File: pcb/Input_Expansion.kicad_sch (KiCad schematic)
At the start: 3 parts, among them U2 MCP23008-xP

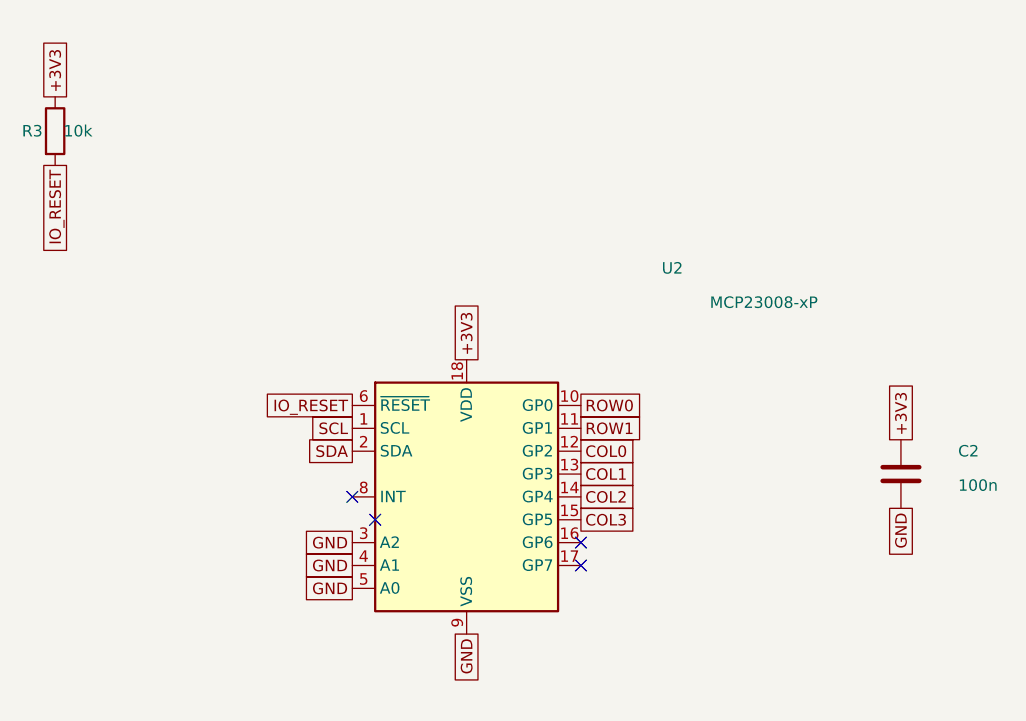
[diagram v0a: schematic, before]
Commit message: Updated wih cheeaper pads
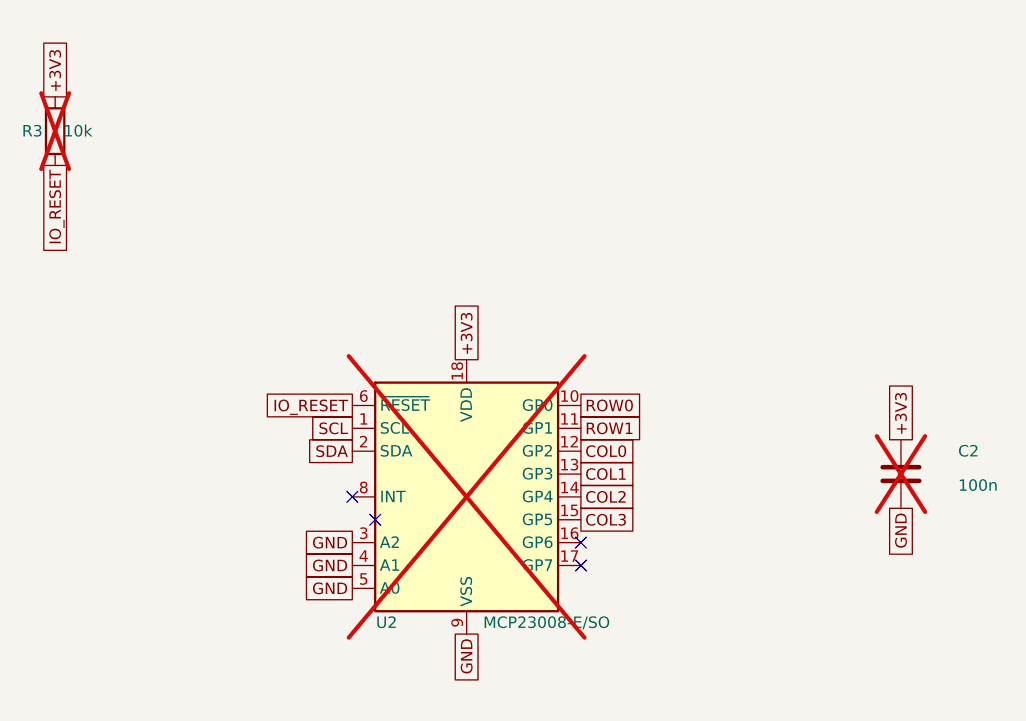
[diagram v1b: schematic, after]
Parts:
- removed U2: MCP23008-xP, Package_DIP:DIP-18_W7.62mm, symbol Interface_Expansion:MCP23008-xP
- added U2: MCP23008-E/SO, Package_SO:SOIC-18W_7.5x11.6mm_P1.27mm, symbol Interface_Expansion:MCP23008-xSO
- C2, R3: now not fitted
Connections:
- net +3V3: now also U2.18 (VDD)
- net COL0: now also U2.12 (GP2)
- net COL1: now also U2.13 (GP3)
- net COL2: now also U2.14 (GP4)
- net COL3: now also U2.15 (GP5)
- net GND: now also U2.3 (A2), U2.4 (A1), U2.5 (A0), U2.9 (VSS)
- net IO_RESET: now also U2.6 (~{RESET})
- net ROW0: now also U2.10 (GP0)
- net ROW1: now also U2.11 (GP1)
- net SCL: now also U2.1 (SCL)
- net SDA: now also U2.2 (SDA)
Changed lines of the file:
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@@
 	(paper "A4")
-	(symbol
-		(lib_id "Interface_Expansion:MCP23008-xP")
-		(at 116.84 88.9 0)
-		(unit 1)
-		(body_style 1)
-		(exclude_from_sim no)
-		(in_bom yes)
-		(on_board yes)
-		(in_pos_files yes)
-		(dnp no)
-		(property "Reference" "U2"
-			(at 139.7 63.5 0)
-			(show_name no)
-			(do_not_autoplace no)
-			(effects
-				(font
-					(size 1.27 1.27)
-				)
-			)
-		)
-		(property "Value" "MCP23008-xP"
-			(at 149.86 67.31 0)
-			(show_name no)
-			(do_not_autoplace no)
-			(effects
-				(font
-					(size 1.27 1.27)
-				)
-			)
-		)
-		(property "Footprint" "Package_DIP:DIP-18_W7.62mm"
-			(at 116.84 62.23 0)
-			(hide yes)
-			(show_name no)
-			(do_not_autoplace no)
-			(effects
-				(font
-					(size 1.27 1.27)
-				)
-			)
-		)
-		(property "Datasheet" "http://ww1.microchip.com/downloads/en/DeviceDoc/MCP23008-MCP23S08-Data-Sheet-20001919F.pdf"
-			(at 149.86 58.42 0)
-			(hide yes)
-			(show_name no)
-			(do_not_autoplace no)
-			(effects
-				(font
-					(size 1.27 1.27)
-				)
-			)
-		)
-		(property "Description" "8-bit I/O expander, I2C, interrupts, PDIP-18"
-			(at 116.84 88.9 0)
-			(hide yes)
-			(show_name no)
-			(do_not_autoplace no)
-			(effects
-				(font
-					(size 1.27 1.27)
-				)
-			)
-		)
-		(pin "1"
-		)
-		(pin "10"
-		)
-		(pin "11"
-		)
-		(pin "12"
-		)
-		(pin "13"
-		)
-		(pin "14"
-		)
-		(pin "15"
-		)
-		(pin "16"
-		)
-		(pin "17"
-		)
-		(pin "18"
-		)
-		(pin "2"
-		)
-		(pin "3"
-		)
-		(pin "4"
-		)
-		(pin "5"
-		)
-		(pin "6"
-		)
-		(pin "7"
-		)
-		(pin "8"
-		)
-		(pin "9"
-		)
-		(instances
-			(project "Fabricate_Wireless_Macropad"
-				(path "/24af3139-98ac-4ed0-b313-5c2ea4f6f921"
-					(reference "U2")
-					(unit 1)
-				)
-				(path "/eae26e58-6f77-4657-abf4-2b51d059bce3/0ae5ae52-a859-4710-ad5e-fe4e0cea6db1"
-					(reference "U2")
-					(unit 1)
-				)
-			)
-		)
-	)
 	(symbol
 		(lib_id "Device:R")
@@
 		(on_board yes)
 		(in_pos_files yes)
-		(dnp no)
+		(dnp yes)
 		(property "Reference" "R3"
 			(at 68.58 48.26 0)
@@
 		(on_board yes)
 		(in_pos_files yes)
-		(dnp no)
+		(dnp yes)
 		(property "Reference" "C2"
 			(at 171.45 83.82 0)
@@
 	)
 	(global_label "SDA"
-		(at 104.14 83.82000000000001 180)
+		(at 104.14 83.82 180)
 		(effects
 			(font
@@
 	)
 	(global_label "GND"
-		(at 104.14 96.52000000000001 180)
+		(at 104.14 96.52 180)
 		(effects
 			(font
@@
 	)
 	(global_label "IO_RESET"
-		(at 104.14 78.74000000000001 180)
+		(at 104.14 78.74 180)
 		(effects
 			(font
@@
 	)
 	(global_label "ROW0"
-		(at 129.54 78.74000000000001 0)
+		(at 129.54 78.74 0)
 		(effects
 			(font
@@
 	)
 	(global_label "COL0"
-		(at 129.54 83.82000000000001 0)
+		(at 129.54 83.82 0)
 		(effects
 			(font
@@
 	)
 	(global_label "COL3"
-		(at 129.54 91.44000000000001 0)
+		(at 129.54 91.44 0)
 		(effects
 			(font
@@
 	)
 	(global_label "+3V3"
-		(at 116.84 73.66000000000001 90)
+		(at 116.84 73.66 90)
 		(effects
 			(font
@@
 	)
 	(global_label "+3V3"
-		(at 71.12 44.449999999999996 90)
+		(at 71.12 44.45 90)
 		(effects
 			(font
@@
 	)
 	(no_connect
-		(at 106.68 91.44000000000001)
+		(at 106.68 91.44)
 	)
 	(no_connect
@@
 	)
 	(no_connect
-		(at 129.54 96.52000000000001)
+		(at 129.54 96.52)
+	)
+	(symbol
+		(lib_id "Interface_Expansion:MCP23008-xSO")
+		(at 116.84 88.9 0)
+		(unit 1)
+		(body_style 1)
+		(exclude_from_sim no)
+		(in_bom yes)
+		(on_board yes)
+		(in_pos_files yes)
+		(dnp yes)
+		(property "Reference" "U2"
+			(at 107.95 102.87 0)
+			(show_name no)
+			(do_not_autoplace no)
+			(effects
+				(font
+					(size 1.27 1.27)
+				)
+			)
+		)
+		(property "Value" "MCP23008-E/SO"
+			(at 125.73 102.87 0)
+			(show_name no)
+			(do_not_autoplace no)
+			(effects
+				(font
+					(size 1.27 1.27)
+				)
+			)
+		)
+		(property "Footprint" "Package_SO:SOIC-18W_7.5x11.6mm_P1.27mm"
+			(at 116.84 62.23 0)
+			(hide yes)
+			(show_name no)
+			(do_not_autoplace no)
+			(effects
+				(font
+					(size 1.27 1.27)
+				)
+			)
+		)
+		(property "Datasheet" "http://ww1.microchip.com/downloads/en/DeviceDoc/MCP23008-MCP23S08-Data-Sheet-20001919F.pdf"
+			(at 149.86 58.42 0)
+			(hide yes)
+			(show_name no)
+			(do_not_autoplace no)
+			(effects
+				(font
+					(size 1.27 1.27)
+				)
+			)
+		)
+		(property "Description" "8-bit I2C I/O expander, SOIC-18 wide, 1.27 mm pitch"
+			(at 116.84 88.9 0)
+			(hide yes)
+			(show_name no)
+			(do_not_autoplace no)
+			(effects
+				(font
+					(size 1.27 1.27)
+				)
+			)
+		)
+		(property "MPN" "MCP23008-E/SO"
+			(at 116.84 88.9 0)
+			(effects
+				(font
+					(size 1.27 1.27)
+				)
+				(hide yes)
+			)
+		)
+		(pin "1"
+		)
+		(pin "10"
+		)
+		(pin "11"
+		)
+		(pin "12"
+		)
+		(pin "13"
+		)
+		(pin "14"
+		)
+		(pin "15"
+		)
+		(pin "16"
+		)
+		(pin "17"
+		)
+		(pin "18"
+		)
+		(pin "2"
+		)
+		(pin "3"
+		)
+		(pin "4"
+		)
+		(pin "5"
+		)
+		(pin "6"
+		)
+		(pin "7"
+		)
+		(pin "8"
+		)
+		(pin "9"
+		)
+		(instances
+			(project "Fabricate_Wireless_Macropad"
+				(path "/eae26e58-6f77-4657-abf4-2b51d059bce3/0ae5ae52-a859-4710-ad5e-fe4e0cea6db1"
+					(reference "U2")
+					(unit 1)
+				)
+			)
+		)
 	)
 	(sheet_instances
